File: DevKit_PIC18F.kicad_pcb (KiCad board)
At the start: 2 copper layers, 41 x 72 mm, 29 parts, among them J1 PIC_ICSP_ICD, J2 USB_B, J3 5P_UART, J4 RA_PORT, J5 RB_PORT, J6 RD_PORT, J7 RC_PORT, J8 RE_PORT, SW1 SW_DIP, X1 16MHz

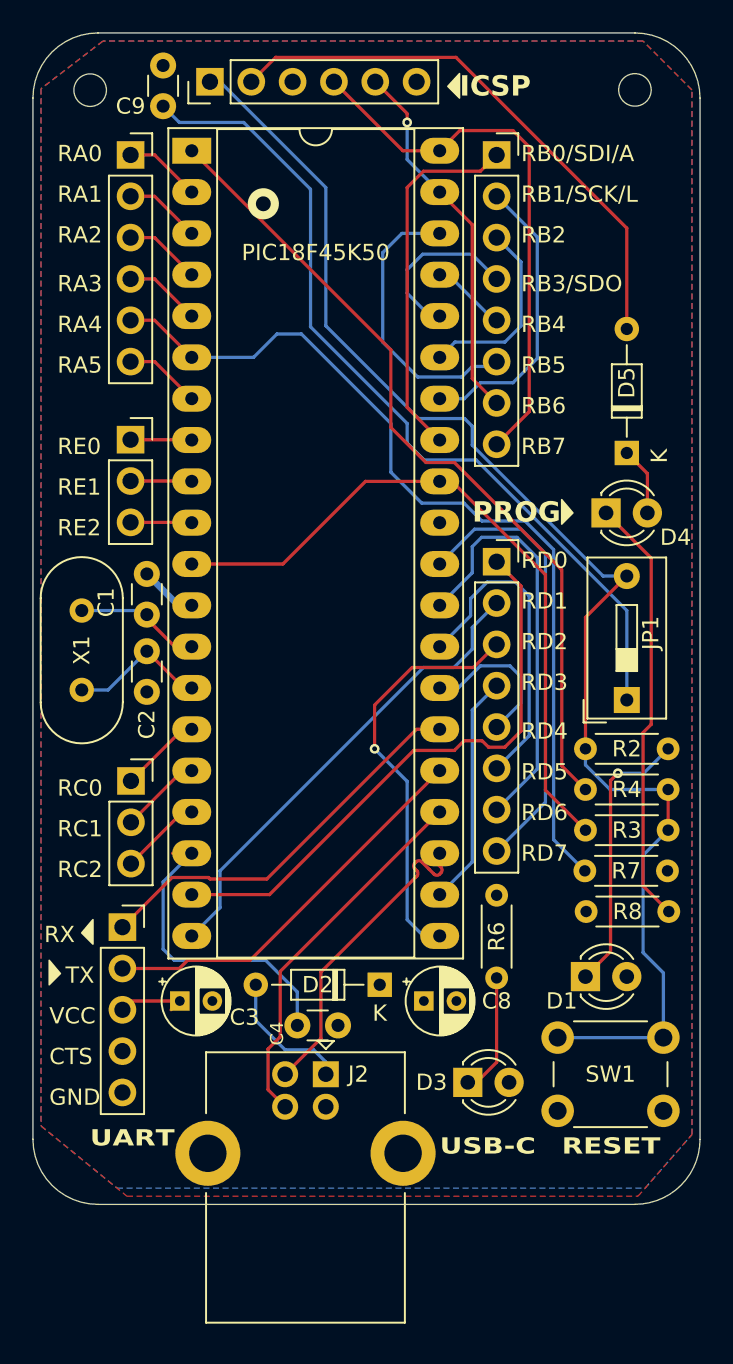
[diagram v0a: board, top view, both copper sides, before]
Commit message: Refine/Fix Short-circuit on USB-B
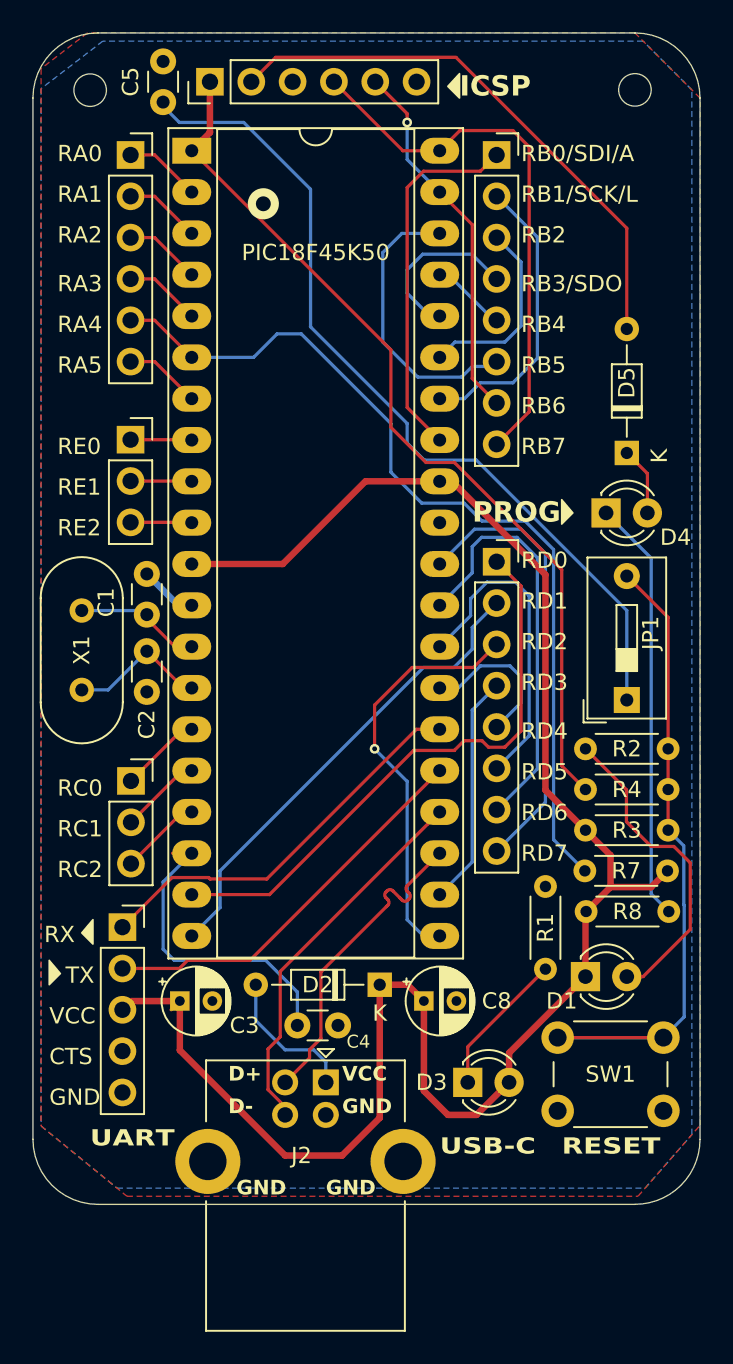
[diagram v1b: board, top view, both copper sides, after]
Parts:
- removed C9: 0.1uF, Capacitor_THT:C_Disc_D3.0mm_W1.6mm_P2.50mm
- removed R6: 330, Resistor_THT:R_Axial_DIN0204_L3.6mm_D1.6mm_P5.08mm_Horizontal
- added C5: 0.1uF, Capacitor_THT:C_Disc_D3.0mm_W1.6mm_P2.50mm, F.Cu at (76.0, 28.2)
- added R1: 330, Resistor_THT:R_Axial_DIN0204_L3.6mm_D1.6mm_P5.08mm_Horizontal, F.Cu at (99.5, 84.0)
- moved J2 0.50 mm to (86.0, 91.0)
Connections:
- C3 pad 1: GND -> VCC
- C8 pad 1: GND -> VCC
- D1 pad 1: Net-(D1-K) -> VCC
- D1 pad 2: GND -> Net-(D1-A)
- D2 pad 1: GND -> VCC
- D3 pad 2: GND -> VCC
- J3 pad 3: GND -> VCC
- JP1 pad 2: /MCLR -> Net-(JP1-B)
- PIC18F45K50 pad 1: Net-(PIC18F45K50-RE3/VPP/*MCLR) -> /MCLR
- PIC18F45K50 pad 11: GND -> VCC
- PIC18F45K50 pad 32: GND -> VCC
- R2 pad 1: Net-(D1-K) -> Net-(JP1-B)
- R2 pad 2: /MCLR -> Net-(D1-A)
- R3 pad 1: GND -> VCC
- R3 pad 2: /MCLR -> Net-(JP1-B)
- R4 pad 1: Net-(PIC18F45K50-RE3/VPP/*MCLR) -> /MCLR
- R4 pad 2: /MCLR -> Net-(JP1-B)
- R7 pad 1: GND -> VCC
- R8 pad 1: GND -> VCC
- SW1 pad 1: /MCLR -> Net-(JP1-B)
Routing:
- net VCC: track 0.00 -> 113.6 mm
- net Net-(PIC18F45K50-RE3/VPP/*MCLR): track 50.9 -> 0.00 mm
- net GND: track 53.2 -> 4.61 mm
- net Net-(JP1-B): track 0.00 -> 44.4 mm
- net /MCLR: track 86.1 -> 56.2 mm
- net Net-(D1-A): track 0.00 -> 19.7 mm
- net Net-(D1-K): track 17.0 -> 0.00 mm, vias 1 -> 0
- net Net-(D3-K): track 7.31 -> 8.94 mm
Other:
- board text added: "D+"
- board text added: "D-"

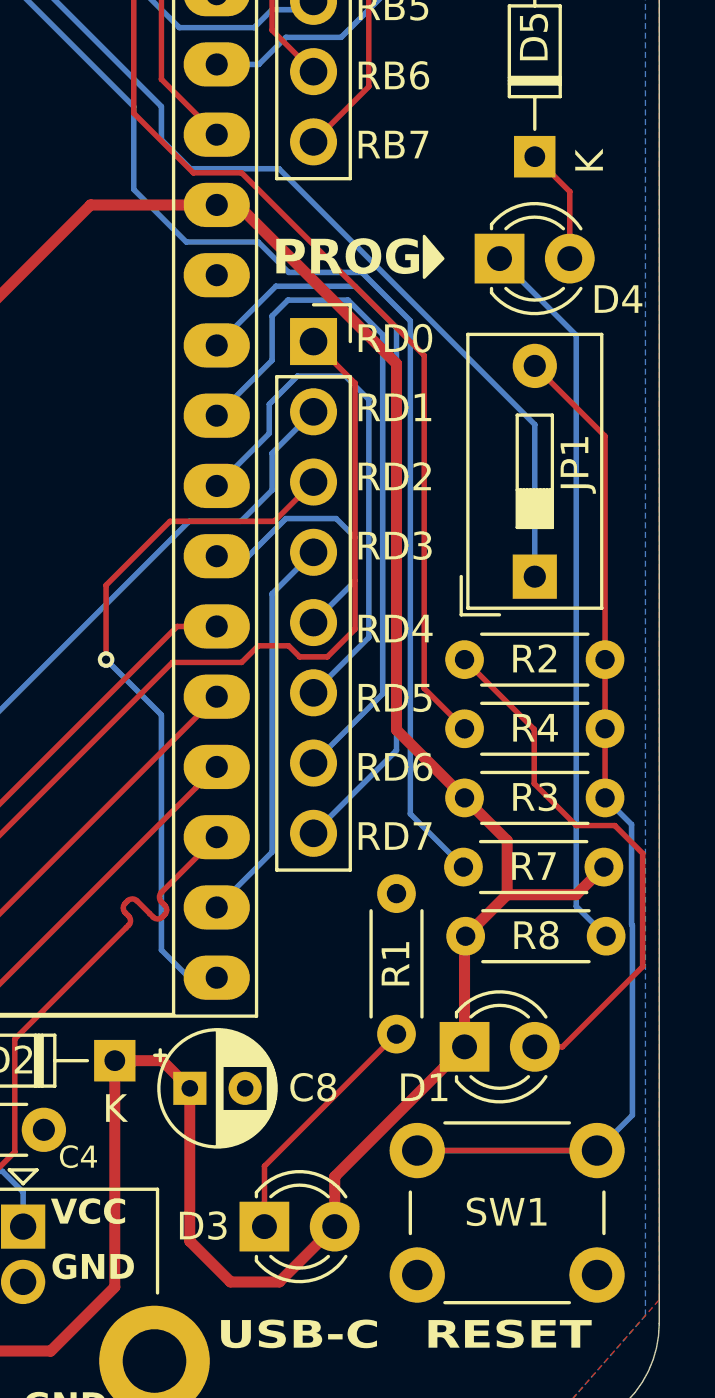
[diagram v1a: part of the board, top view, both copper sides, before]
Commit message: Fix Bug : remove bridge as we don't need it.
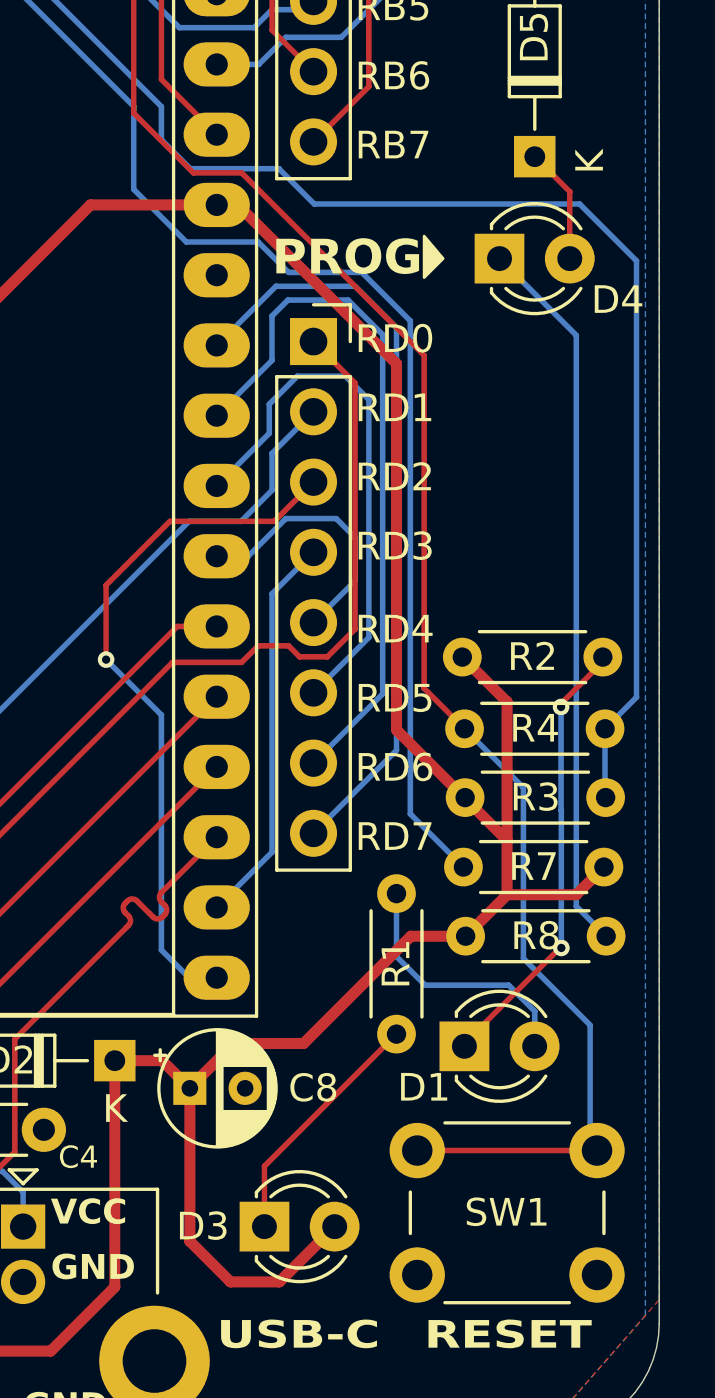
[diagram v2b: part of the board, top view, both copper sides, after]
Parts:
- removed JP1: JP_MLCR, Button_Switch_THT:SW_DIP_SPSTx01_Slide_9.78x4.72mm_W7.62mm_P2.54mm
- C5: value 0.1uF -> 10uF
- D1: value LED_RST -> LED_PWR
- SW1: value SW_DIP -> SW_RST
- moved R2 0.12 mm to (107.0, 70.4)
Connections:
- C5 pad 2: Net-(JP1-A) -> Net-(C5-Pad2)
- D1 pad 1: VCC -> Net-(D1-K)
- D1 pad 2: Net-(D1-A) -> GND
- R2 pad 1: Net-(JP1-B) -> Net-(D1-K)
- R2 pad 2: Net-(D1-A) -> VCC
- R3 pad 2: Net-(JP1-B) -> Net-(C5-Pad2)
- R4 pad 2: Net-(JP1-B) -> Net-(C5-Pad2)
- SW1 pad 1: Net-(JP1-B) -> /MCLR
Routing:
- net Net-(C5-Pad2): track 0.00 -> 67.6 mm
- net Net-(JP1-A): track 52.5 -> 0.00 mm
- net Net-(JP1-B): track 44.4 -> 0.00 mm
- net /MCLR: track 56.2 -> 79.9 mm
- net Net-(D1-A): track 19.7 -> 0.00 mm
- net Net-(D1-K): track 0.00 -> 15.4 mm, vias 0 -> 2
- net GND: track 4.61 -> 14.0 mm
- net VCC: track 113.6 -> 121.1 mm

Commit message: update rev -> rev.3 13th Jan, 2025: remove bridge
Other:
- board text added: "DevKit PIC18F45XX Rev.3 : 13th Jan, 2025 Designed by @deulamco"
- board text removed: "DevKit PIC18F45XX Rev.1 : 23th Sep, 2024 Designed by @deulamco"

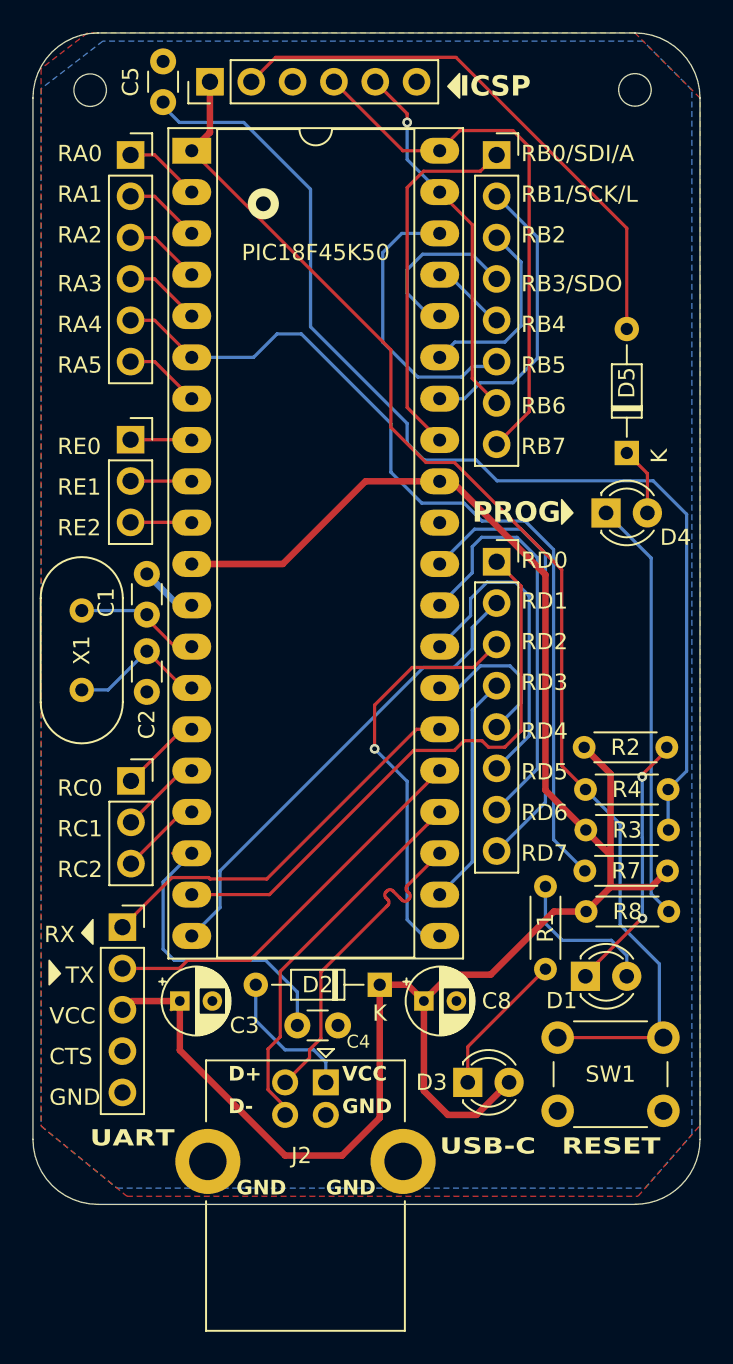
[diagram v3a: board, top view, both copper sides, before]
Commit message: Updaet Rev.4 : Flip:ICSP+ Move->LED, +Test_LED->RD0, Group all Resistors.
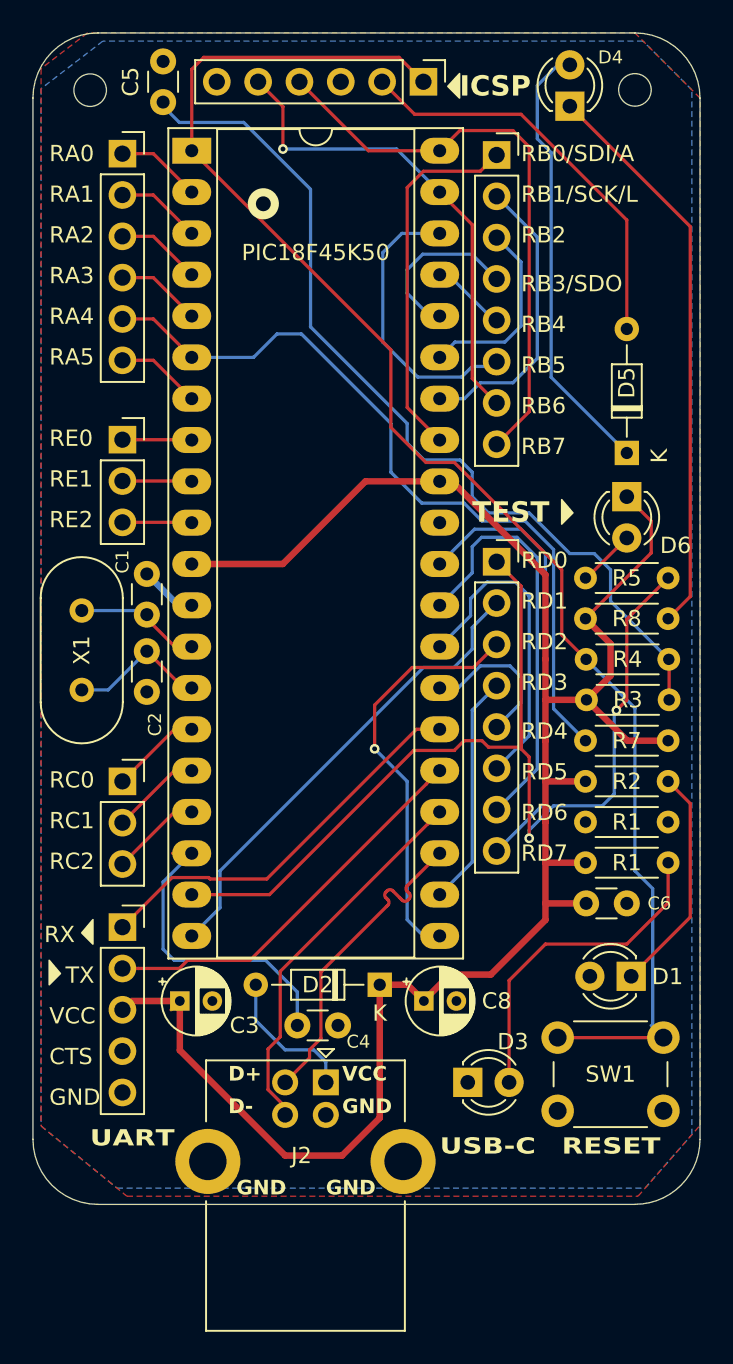
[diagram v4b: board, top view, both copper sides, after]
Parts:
- added C6: 100uF, Capacitor_THT:C_Disc_D3.0mm_W1.6mm_P2.50mm, F.Cu at (104.5, 80.0)
- added D6: LED_VDD, LED_THT:LED_D3.0mm_FlatTop, F.Cu at (104.5, 55.0)
- added R1: 330, Resistor_THT:R_Axial_DIN0204_L3.6mm_D1.6mm_P5.08mm_Horizontal, F.Cu at (102.0, 77.5)
- added R5: 330, Resistor_THT:R_Axial_DIN0204_L3.6mm_D1.6mm_P5.08mm_Horizontal, F.Cu at (107.0, 60.0)
- moved D4 25.1 mm to (101.0, 31.0), turned to 90 degrees
- moved R8 18.0 mm to (102.0, 62.5)
- moved J1 13.1 mm to (92.0, 29.5), turned to -90 degrees
- moved R1 11.8 mm to (107.0, 75.0), turned to 180 degrees
- moved R3 8.00 mm to (102.0, 67.5)
- moved R4 8.00 mm to (102.0, 65.0)
- moved R7 8.00 mm to (107.0, 70.0)
- moved D1 2.81 mm to (104.8, 84.5), turned to 180 degrees
- moved R2 2.09 mm to (107.0, 72.5)
- moved J7 0.53 mm to (73.5, 72.5)
- moved J4 0.51 mm to (73.5, 33.9)
- moved J8 0.50 mm to (73.5, 51.5)
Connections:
- D3 pad 1: Net-(D3-K) -> GND
- D3 pad 2: VCC -> Net-(D3-A)
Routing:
- net Net-(J6-Pin_1): track 35.8 -> 64.4 mm, vias 0 -> 2
- net Net-(D4-A): track 4.21 -> 27.4 mm
- net Net-(D3-A): track 0.00 -> 20.6 mm
- net /MCLR: track 79.9 -> 95.6 mm
- net Net-(C5-Pad2): track 67.6 -> 55.3 mm
- net GND: track 14.0 -> 4.61 mm
- net Net-(D5-A): track 34.2 -> 25.3 mm
- net Net-(D3-K): track 8.94 -> 0.00 mm
- net Net-(D4-K): track 26.4 -> 35.1 mm
- net Net-(J4-Pin_5): track 55.4 -> 47.4 mm
- net /PGC: track 22.8 -> 29.9 mm
- net VCC: track 121.1 -> 125.2 mm
- net Net-(D6-A): track 0.00 -> 3.56 mm
- net /PGD: track 33.8 -> 35.9 mm
- net Net-(D1-K): track 15.4 -> 14.0 mm, vias 2 -> 0
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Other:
- board text added: "DevKit PIC18F45XX Rev.4 : 22th Feb, 2025 Designed by @deulamco"
- board text added: "TEST"
- board text removed: "DevKit PIC18F45XX Rev.3 : 13th Jan, 2025 Designed by @deulamco"
- board text removed: "PROG"

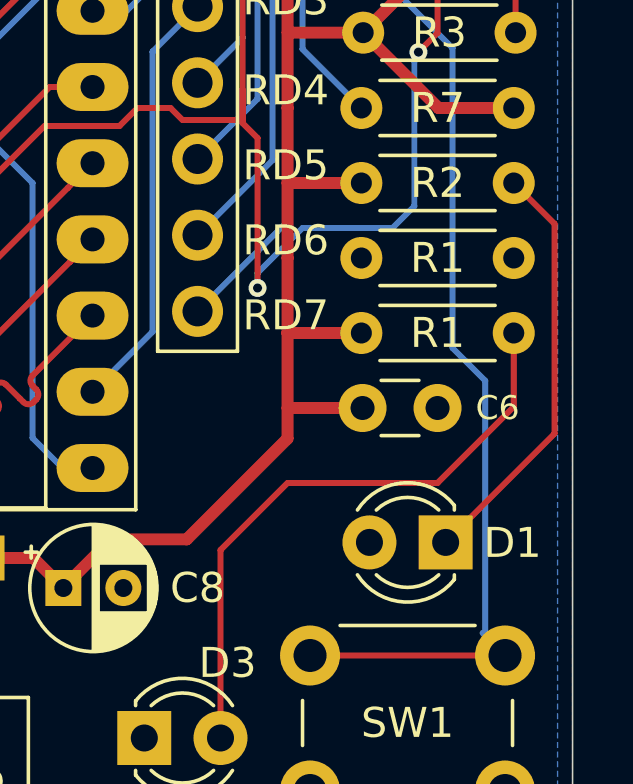
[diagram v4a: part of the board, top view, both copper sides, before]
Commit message: Rev.5 : remove redundant LED D1
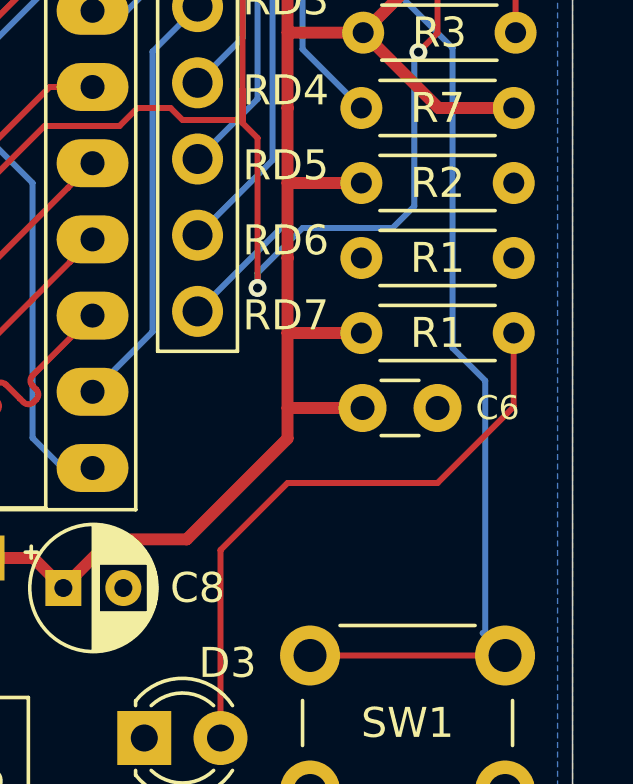
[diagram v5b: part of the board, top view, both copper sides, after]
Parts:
- removed D1: LED_PWR, LED_THT:LED_D3.0mm_FlatTop
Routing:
- net Net-(D1-K): track 14.0 -> 0.00 mm
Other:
- board text added: "DevKit PIC18F45XX Rev.5 : 22th Feb, 2025 Designed by @deulamco"
- board text removed: "DevKit PIC18F45XX Rev.4 : 22th Feb, 2025 Designed by @deulamco"

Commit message: merged changes
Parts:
- removed the R1 at (107.0, 75.0)
- removed R2: 330, Resistor_THT:R_Axial_DIN0204_L3.6mm_D1.6mm_P5.08mm_Horizontal
- moved R1 5.00 mm to (102.0, 72.5)
- moved C6 2.75 mm to (104.5, 77.2), turned to 90 degrees
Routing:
- net Net-(D3-A): track 20.6 -> 25.6 mm
- net Net-(J6-Pin_1): track 64.4 -> 65.4 mm
